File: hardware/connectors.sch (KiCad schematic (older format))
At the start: 16 parts

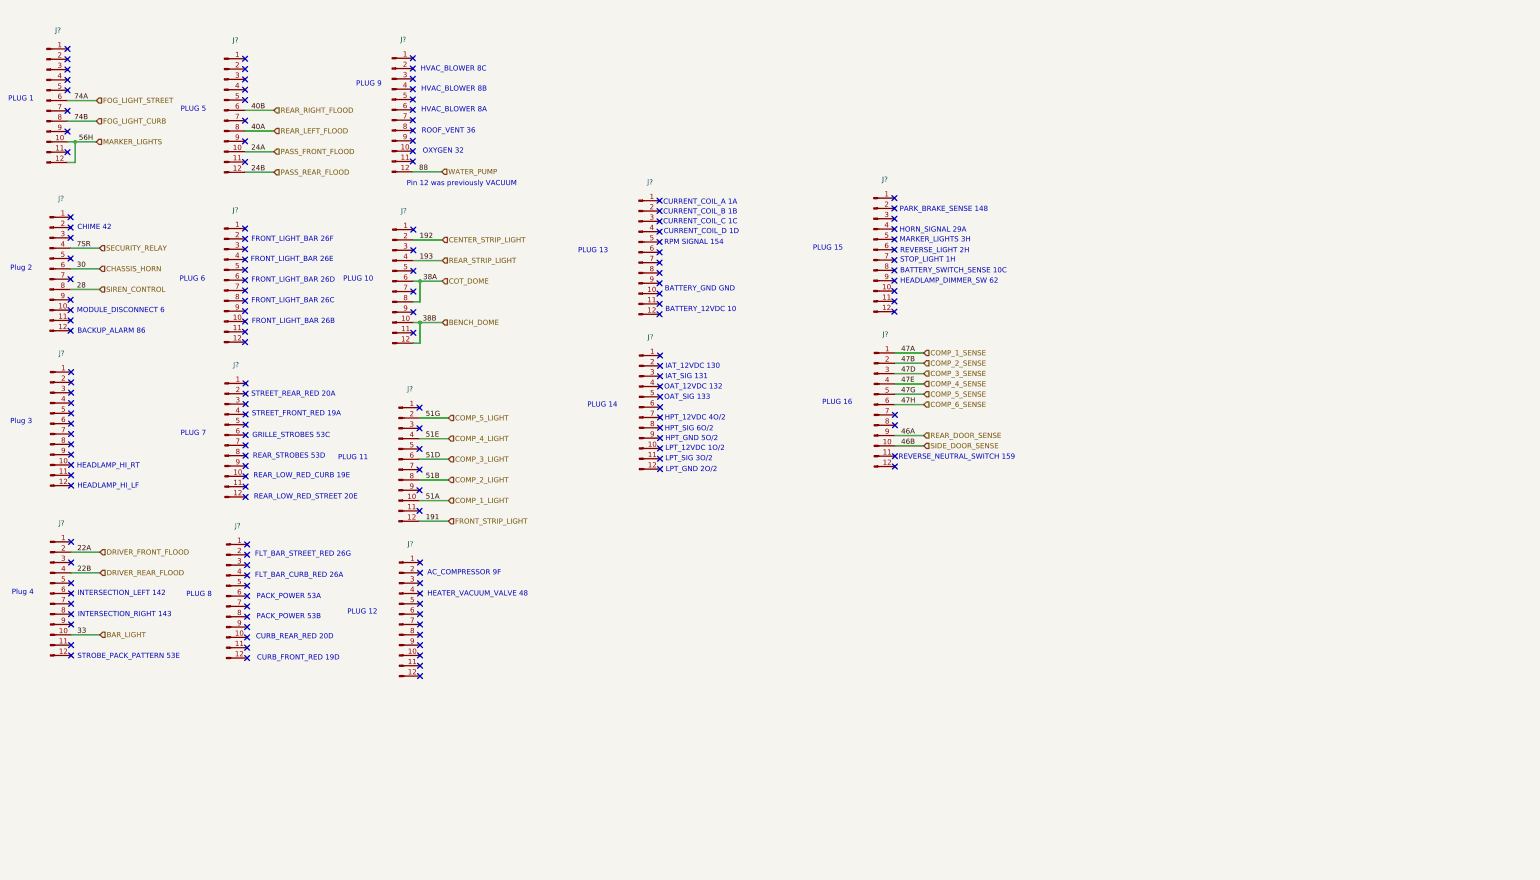
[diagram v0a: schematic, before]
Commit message: hardware: export connectors connections
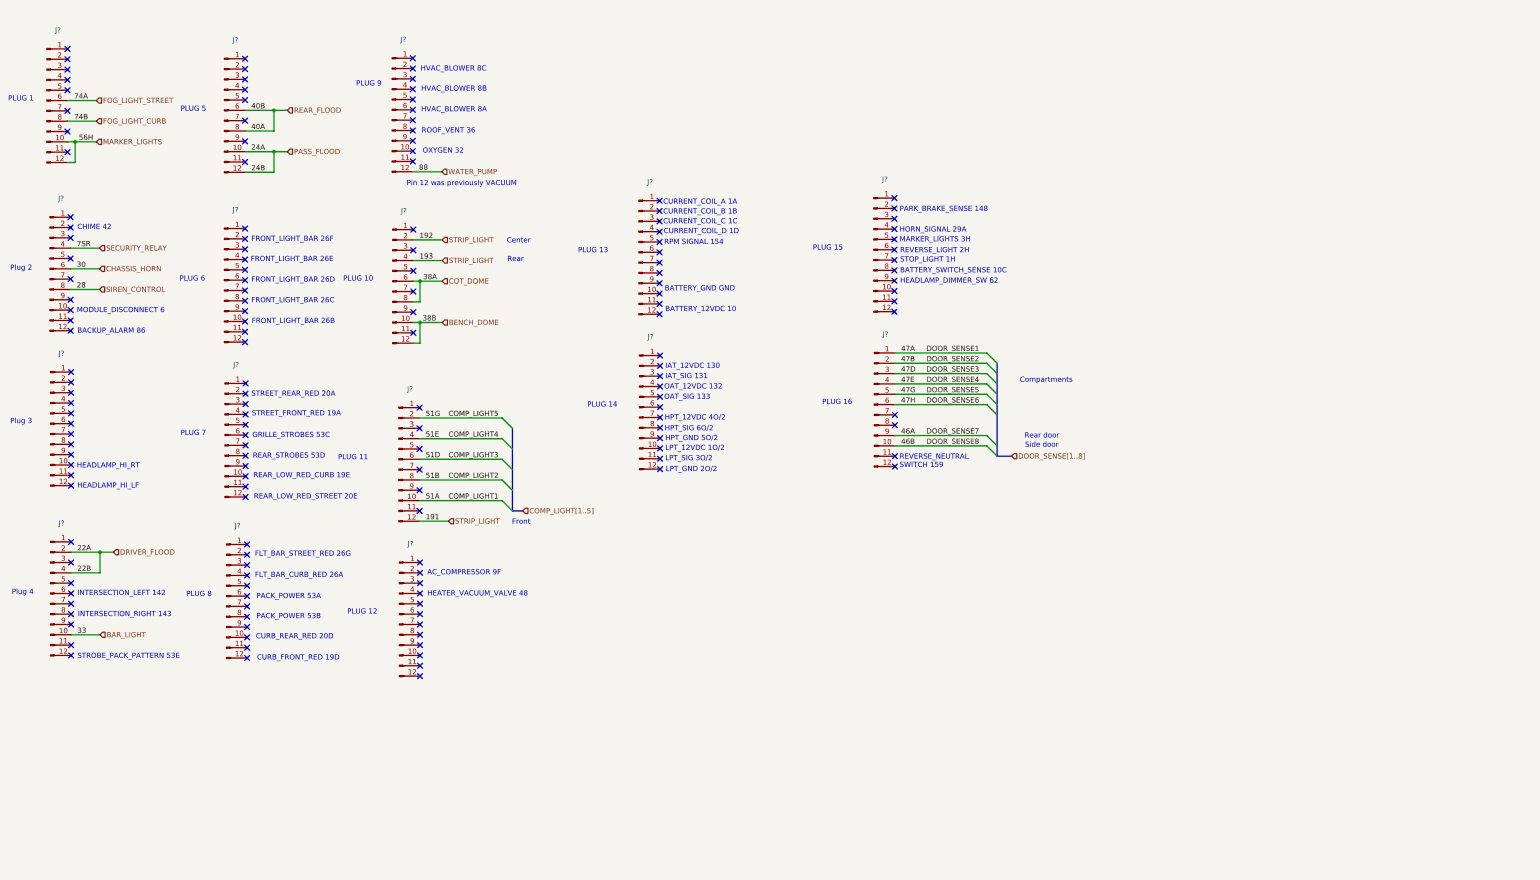
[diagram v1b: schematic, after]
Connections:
- net DRIVER_REAR_FLOOD is gone; now on net DRIVER_FLOOD: J?.4 (Pin_4)
- net FRONT_STRIP_LIGHT is gone; now on net STRIP_LIGHT: J?.12 (Pin_12)
- net PASS_REAR_FLOOD is gone; now on net PASS_FLOOD: J?.12 (Pin_12)
- net REAR_RIGHT_FLOOD is gone; now on net REAR_FLOOD: J?.6 (Pin_6)
- net REAR_STRIP_LIGHT is gone; now on net STRIP_LIGHT: J?.4 (Pin_4)
- net CENTER_STRIP_LIGHT renamed STRIP_LIGHT
- net COMP_1_LIGHT renamed 51A
- net COMP_1_SENSE renamed 47A
- net COMP_2_LIGHT renamed 51B
- net COMP_2_SENSE renamed 47B
- net COMP_3_LIGHT renamed 51D
- net COMP_3_SENSE renamed 47D
- net COMP_4_LIGHT renamed 51E
- net COMP_4_SENSE renamed 47E
- net COMP_5_LIGHT renamed 51G
- net COMP_5_SENSE renamed 47G
- net COMP_6_SENSE renamed 47H
- net DRIVER_FRONT_FLOOD renamed DRIVER_FLOOD
- net PASS_FRONT_FLOOD renamed PASS_FLOOD
- net REAR_DOOR_SENSE renamed 46A
- net REAR_LEFT_FLOOD renamed REAR_FLOOD
- net SIDE_DOOR_SENSE renamed 46B
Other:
- note added: "Center"
- note added: "Compartments"
- note added: "Front"
- note added: "REVERSE_NEUTRAL\nSWITCH 159"
- note added: "Rear"
- note added: "Rear door"
- note added: "Side door"
- note removed: "REVERSE_NEUTRAL_SWITCH 159"
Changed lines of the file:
@@
 $Descr A4 11693 8268
 encoding utf-8
-Sheet 3 6
+Sheet 6 6
 Title ""
 Date ""
@@
 Wire Wire Line
 	1245 6835 1525 6835
-Wire Wire Line
-	2930 2155 3210 2155
-Text HLabel 3210 2155 2    50   Input ~ 0
-PASS_FRONT_FLOOD
-Wire Wire Line
-	2930 2355 3210 2355
-Text HLabel 3210 2355 2    50   Input ~ 0
-PASS_REAR_FLOOD
 Text Label 2990 2355 0    50   ~ 0
 24B
@@
 Wire Wire Line
 	2930 1755 3210 1755
-Text HLabel 3210 1755 2    50   Input ~ 0
-REAR_RIGHT_FLOOD
+Text HLabel 3340 1755 2    50   Input ~ 0
+REAR_FLOOD
 Wire Wire Line
 	2930 1955 3210 1955
-Text HLabel 3210 1955 2    50   Input ~ 0
-REAR_LEFT_FLOOD
 Text Label 2990 1955 0    50   ~ 0
 40A
@@
 	4560 3210 4840 3210
 Text HLabel 4840 3210 2    50   Input ~ 0
-REAR_STRIP_LIGHT
+STRIP_LIGHT
 Text Label 4620 3210 0    50   ~ 0
 193
@@
 	4560 3010 4840 3010
 Text HLabel 4840 3010 2    50   Input ~ 0
-CENTER_STRIP_LIGHT
+STRIP_LIGHT
 Text Label 4620 3010 0    50   ~ 0
 192
@@
 NoConn ~ 4560 3110
 NoConn ~ 4560 2910
-Wire Wire Line
-	4620 5735 4900 5735
-Text HLabel 4900 5735 2    50   Input ~ 0
-FRONT_STRIP_LIGHT
 Text Label 4680 5735 0    50   ~ 0
 191
-Wire Wire Line
-	4620 5535 4900 5535
-Text HLabel 4900 5535 2    50   Input ~ 0
-COMP_1_LIGHT
 Text Label 4680 5535 0    50   ~ 0
 51A
-Wire Wire Line
-	4620 5335 4900 5335
-Text HLabel 4900 5335 2    50   Input ~ 0
-COMP_2_LIGHT
 Text Label 4680 5335 0    50   ~ 0
 51B
-Wire Wire Line
-	4620 5135 4900 5135
-Text HLabel 4900 5135 2    50   Input ~ 0
-COMP_3_LIGHT
 Text Label 4680 5135 0    50   ~ 0
 51D
-Wire Wire Line
-	4620 4935 4900 4935
-Text HLabel 4900 4935 2    50   Input ~ 0
-COMP_4_LIGHT
 Text Label 4680 4935 0    50   ~ 0
 51E
 Wire Wire Line
-	4620 4735 4900 4735
-Text HLabel 4900 4735 2    50   Input ~ 0
-COMP_5_LIGHT
+	4620 4735 5420 4735
 Text Label 4680 4735 0    50   ~ 0
 51G
@@
 NoConn ~ 4620 4835
 NoConn ~ 4620 4635
-Wire Wire Line
-	9225 4105 9505 4105
-Text HLabel 9505 4105 2    50   Input ~ 0
-COMP_1_SENSE
 Text Label 9285 4105 0    50   ~ 0
 47A
 Wire Wire Line
-	9225 4205 9505 4205
-Text HLabel 9505 4205 2    50   Input ~ 0
-COMP_2_SENSE
+	9225 4205 10115 4205
 Text Label 9285 4205 0    50   ~ 0
 47B
 Wire Wire Line
-	9225 4305 9505 4305
-Text HLabel 9505 4305 2    50   Input ~ 0
-COMP_3_SENSE
+	9225 4305 10115 4305
 Text Label 9285 4305 0    50   ~ 0
 47D
 Wire Wire Line
-	9225 4405 9505 4405
-Text HLabel 9505 4405 2    50   Input ~ 0
-COMP_4_SENSE
+	9225 4405 10115 4405
 Text Label 9285 4405 0    50   ~ 0
 47E
 Wire Wire Line
-	9225 4505 9505 4505
-Text HLabel 9505 4505 2    50   Input ~ 0
-COMP_5_SENSE
+	9225 4505 10115 4505
 Text Label 9285 4505 0    50   ~ 0
 47G
 Wire Wire Line
-	9225 4605 9505 4605
-Text HLabel 9505 4605 2    50   Input ~ 0
-COMP_6_SENSE
+	9225 4605 10115 4605
 Text Label 9285 4605 0    50   ~ 0
 47H
-Wire Wire Line
-	9225 4905 9505 4905
-Text HLabel 9505 4905 2    50   Input ~ 0
-REAR_DOOR_SENSE
 Text Label 9285 4905 0    50   ~ 0
 46A
-Wire Wire Line
-	9225 5005 9505 5005
-Text HLabel 9505 5005 2    50   Input ~ 0
-SIDE_DOOR_SENSE
 Text Label 9285 5005 0    50   ~ 0
 46B
@@
 NoConn ~ 9225 5105
 NoConn ~ 9225 5205
-Text Notes 9260 5145 0    50   ~ 0
-REVERSE_NEUTRAL_SWITCH 159
+Text Notes 9270 5225 0    50   ~ 0
+REVERSE_NEUTRAL\nSWITCH 159
 Text Notes 4695 6265 0    50   ~ 0
 AC_COMPRESSOR 9F
@@
 Text Label 1305 6235 0    50   ~ 0
 22B
-Text HLabel 1525 6235 2    50   Input ~ 0
-DRIVER_REAR_FLOOD
-Wire Wire Line
-	1245 6235 1525 6235
 Text Label 1305 6035 0    50   ~ 0
 22A
-Text HLabel 1525 6035 2    50   Input ~ 0
-DRIVER_FRONT_FLOOD
+Wire Wire Line
+	3210 1955 3210 1755
+Wire Wire Line
+	3210 1755 3340 1755
+Connection ~ 3210 1755
+Wire Wire Line
+	2930 2155 3210 2155
+Text HLabel 3340 2155 2    50   Input ~ 0
+PASS_FLOOD
+Wire Wire Line
+	2930 2355 3210 2355
+Wire Wire Line
+	3210 2355 3210 2155
+Wire Wire Line
+	3210 2155 3340 2155
+Connection ~ 3210 2155
 Wire Wire Line
 	1245 6035 1525 6035
+Text HLabel 1655 6035 2    50   Input ~ 0
+DRIVER_FLOOD
+Wire Wire Line
+	1245 6235 1525 6235
+Wire Wire Line
+	1525 6235 1525 6035
+Wire Wire Line
+	1525 6035 1655 6035
+Connection ~ 1525 6035
+Wire Wire Line
+	9225 4105 10115 4105
+Text Label 9530 4105 0    50   ~ 0
+DOOR_SENSE1
+Text Label 9530 4205 0    50   ~ 0
+DOOR_SENSE2
+Text Label 9530 4305 0    50   ~ 0
+DOOR_SENSE3
+Text Label 9530 4405 0    50   ~ 0
+DOOR_SENSE4
+Text Label 9530 4505 0    50   ~ 0
+DOOR_SENSE5
+Text Label 9530 4605 0    50   ~ 0
+DOOR_SENSE6
+Entry Wire Line
+	10115 4105 10215 4205
+Entry Wire Line
+	10115 4205 10215 4305
+Entry Wire Line
+	10115 4305 10215 4405
+Entry Wire Line
+	10115 4405 10215 4505
+Entry Wire Line
+	10115 4505 10215 4605
+Entry Wire Line
+	10115 4605 10215 4705
+Entry Wire Line
+	10115 5005 10215 5105
+Entry Wire Line
+	10115 4905 10215 5005
+Text Label 9530 5005 0    50   ~ 0
+DOOR_SENSE8
+Text Label 9530 4905 0    50   ~ 0
+DOOR_SENSE7
+Wire Wire Line
+	9225 5005 10115 5005
+Wire Wire Line
+	9225 4905 10115 4905
+Text Notes 10480 4940 0    50   ~ 0
+Rear door
+Text Notes 10485 5030 0    50   ~ 0
+Side door
+Text Notes 10435 4400 0    50   ~ 0
+Compartments
+Wire Bus Line
+	10215 5105 10355 5105
+Text HLabel 10355 5105 2    50   Input ~ 0
+DOOR_SENSE[1..8]
+Wire Wire Line
+	4620 5735 4900 5735
+Text HLabel 4900 5735 2    50   Input ~ 0
+STRIP_LIGHT
+Text Notes 5515 5775 0    50   ~ 0
+Front
+Text Notes 5465 3050 0    50   ~ 0
+Center
+Text Notes 5470 3230 0    50   ~ 0
+Rear
+Text Label 4900 4735 0    50   ~ 0
+COMP_LIGHT5
+Wire Wire Line
+	4620 4935 5420 4935
+Text Label 4900 4935 0    50   ~ 0
+COMP_LIGHT4
+Wire Wire Line
+	4620 5135 5420 5135
+Text Label 4900 5135 0    50   ~ 0
+COMP_LIGHT3
+Wire Wire Line
+	4620 5335 5420 5335
+Text Label 4900 5335 0    50   ~ 0
+COMP_LIGHT2
+Wire Wire Line
+	4620 5535 5420 5535
+Text Label 4900 5535 0    50   ~ 0
+COMP_LIGHT1
+Entry Wire Line
+	5420 5535 5520 5635
+Entry Wire Line
+	5420 5335 5520 5435
+Entry Wire Line
+	5420 5135 5520 5235
+Entry Wire Line
+	5420 4935 5520 5035
+Entry Wire Line
+	5420 4735 5520 4835
+Wire Bus Line
+	5520 5635 5620 5635
+Text HLabel 5620 5635 2    50   Input ~ 0
+COMP_LIGHT[1..5]
+Wire Bus Line
+	5520 4835 5520 5635
+Wire Bus Line
+	10215 4205 10215 5105
 $EndSCHEMATC
